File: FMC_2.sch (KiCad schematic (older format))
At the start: 14 parts, among them P2 SAMTEC_ASP-134603-01

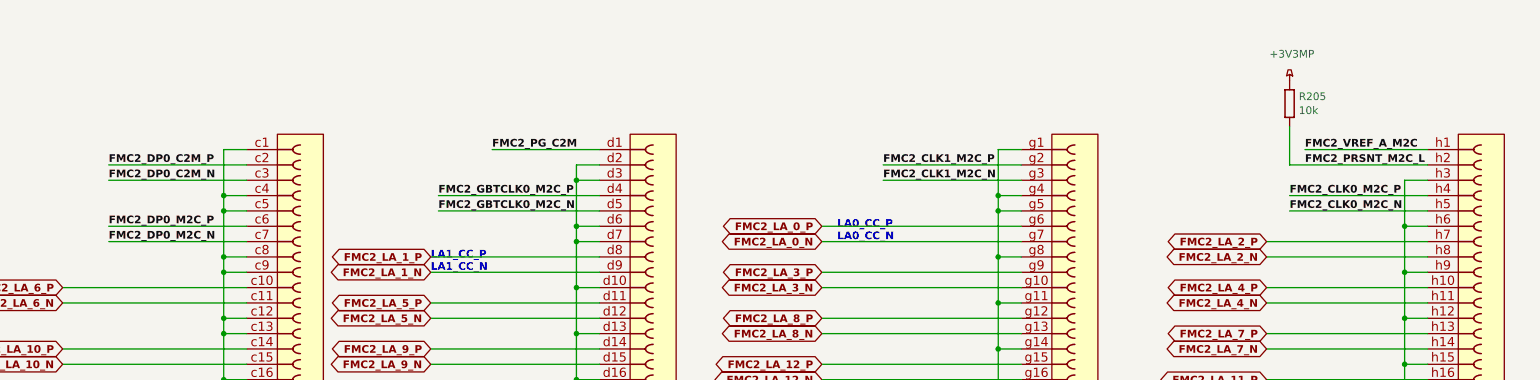
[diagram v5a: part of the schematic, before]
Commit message: new FMC JTAG chain
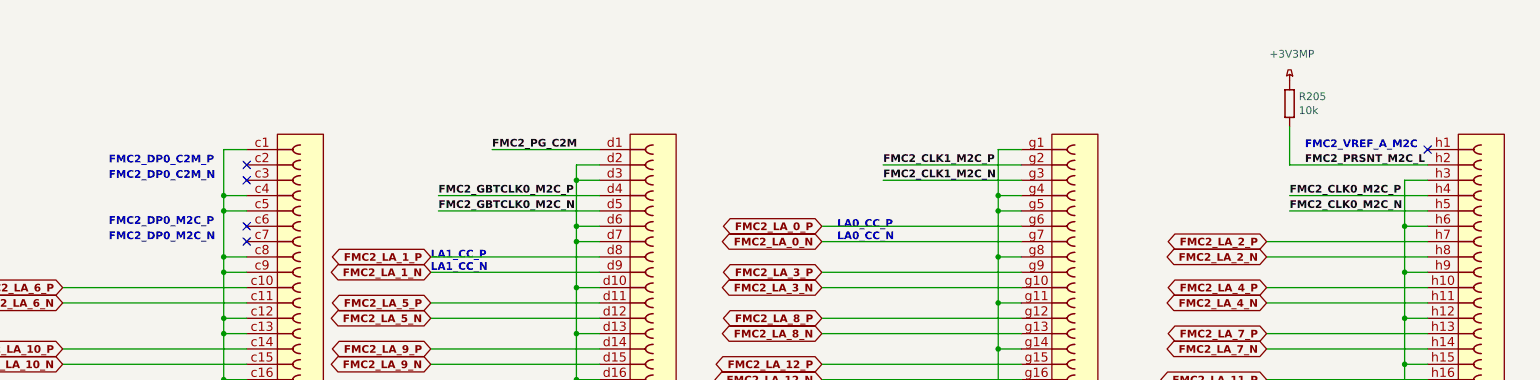
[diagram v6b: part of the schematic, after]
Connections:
- net FMC2_DP0_C2M_N: no longer names the net of P2.c3
- net FMC2_DP0_C2M_P: no longer names the net of P2.c2
- net FMC2_DP0_M2C_N: no longer names the net of P2.c7
- net FMC2_DP0_M2C_P: no longer names the net of P2.c6
- net FMC2_VREF_A_M2C: no longer names the net of P2.h1
- no-connect marks 0 -> 5
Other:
- note added: "FMC2_DP0_C2M_N"
- note added: "FMC2_DP0_C2M_P"
- note added: "FMC2_DP0_M2C_N"
- note added: "FMC2_DP0_M2C_P"
- note added: "FMC2_VREF_A_M2C"
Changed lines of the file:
@@
 Wire Wire Line
 	11400 5450 11400 5750
-Text Label 2950 2050 0    50   ~ 10
-FMC2_DP0_C2M_P
-Text Label 2950 2150 0    50   ~ 10
-FMC2_DP0_C2M_N
-Text Label 2950 2450 0    50   ~ 10
-FMC2_DP0_M2C_P
-Text Label 2950 2550 0    50   ~ 10
-FMC2_DP0_M2C_N
 Text Label 3150 4050 0    50   ~ 10
 FMC2_P_LA_18
@@
 Wire Wire Line
 	3150 4950 3850 4950
-Wire Wire Line
-	2950 2050 3850 2050
-Wire Wire Line
-	2950 2150 3850 2150
-Wire Wire Line
-	2950 2450 3850 2450
-Wire Wire Line
-	2950 2550 3850 2550
 Text Notes 2700 4150 0    50   ~ 10
 LA18_CC_P\nLA18_CC_N
@@
 Text Label 5450 5150 0    50   ~ 10
 FMC2_TMS
-Text Label 5450 5250 0    50   ~ 10
-FMC2_TRST
 Text Label 5450 5350 0    50   ~ 10
 GA1_2
@@
 Wire Wire Line
 	5450 5150 6150 5150
-Wire Wire Line
-	5450 5250 6150 5250
 Wire Wire Line
 	5450 5350 6150 5350
@@
 Text Label 8000 2150 0    50   ~ 10
 FMC2_CLK1_M2C_N
-Text Label 10750 1950 0    50   ~ 10
-FMC2_VREF_A_M2C
 Text Label 10750 2050 0    50   ~ 10
 FMC2_PRSNT_M2C_L
@@
 Wire Wire Line
 	8000 2150 8900 2150
-Wire Wire Line
-	10750 1950 11550 1950
 Wire Wire Line
 	10650 2250 11550 2250
@@
 	-1   0    0    1
 $EndComp
+Text Notes 2950 2050 0    50   ~ 10
+FMC2_DP0_C2M_P
+Text Notes 2950 2150 0    50   ~ 10
+FMC2_DP0_C2M_N
+Text Notes 2950 2450 0    50   ~ 10
+FMC2_DP0_M2C_P
+Text Notes 2950 2550 0    50   ~ 10
+FMC2_DP0_M2C_N
+NoConn ~ 3850 2050
+NoConn ~ 3850 2150
+NoConn ~ 3850 2450
+NoConn ~ 3850 2550
+NoConn ~ 11550 1950
+Text Notes 10750 1950 0    50   ~ 10
+FMC2_VREF_A_M2C
+Text Label 5450 5250 0    50   ~ 10
+FMC2_TRST
+Wire Wire Line
+	5450 5250 6150 5250
 $EndSCHEMATC

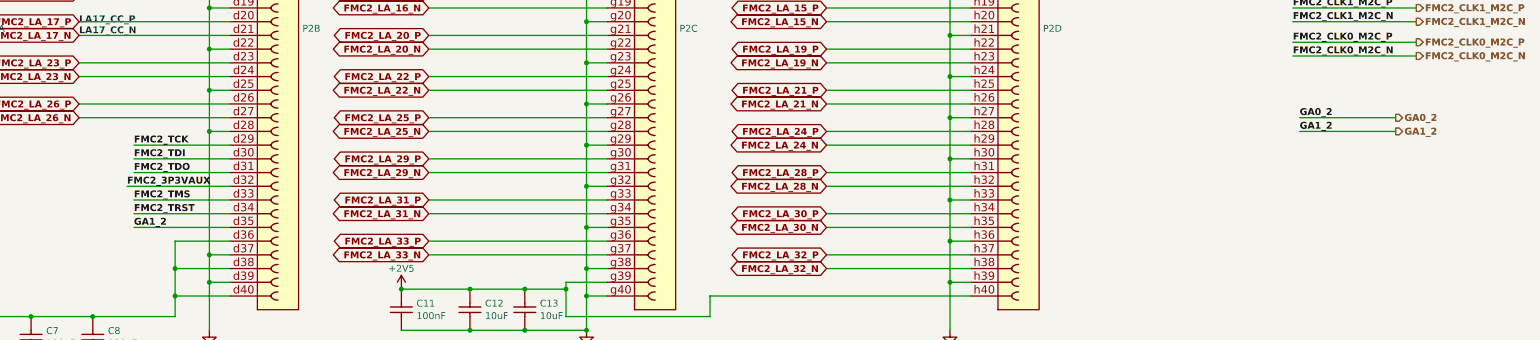
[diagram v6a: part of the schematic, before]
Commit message: JTAG improvrmrnt, bugs fixed
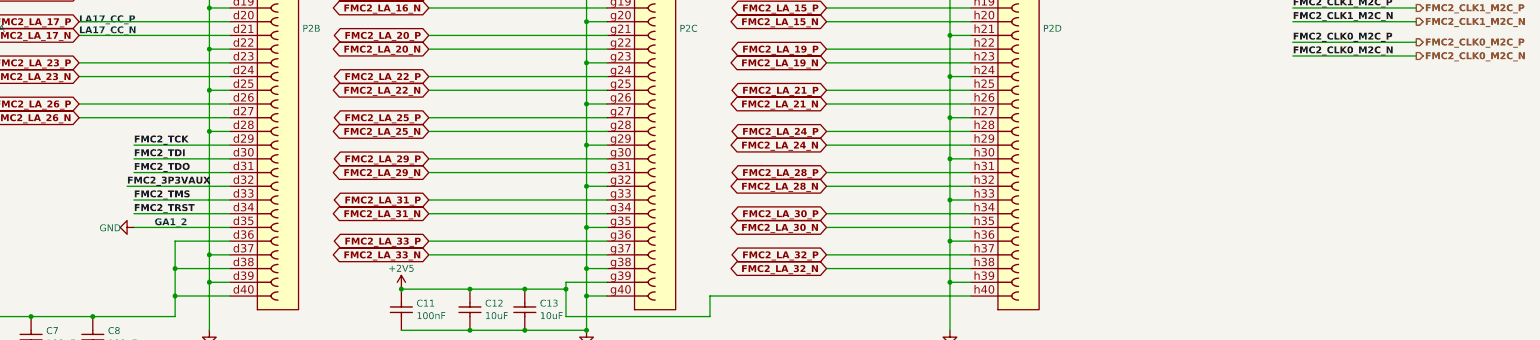
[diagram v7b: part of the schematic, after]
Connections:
- net GA1_2 is gone; now on net GND: P2.d35
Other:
- note added: "GA1_2"
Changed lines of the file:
@@
 Comp "Michał Gąska / WUT"
 Comment1 ""
-Comment2 "FMC 2 connector"
-Comment3 ""
+Comment2 ""
+Comment3 "FMC 2 connector"
 Comment4 ""
 $EndDescr
@@
 Text Label 5450 5150 0    50   ~ 10
 FMC2_TMS
-Text Label 5450 5350 0    50   ~ 10
-GA1_2
 Wire Wire Line
 	5450 1950 6150 1950
@@
 Wire Wire Line
 	13900 4100 14800 4100
-Text Label 13950 4550 0    50   ~ 10
-GA0_2
-Wire Wire Line
-	13950 4550 14650 4550
-Text Label 13950 4650 0    50   ~ 10
-GA1_2
-Wire Wire Line
-	13950 4650 14650 4650
 Text HLabel 14800 3500 2    50   Output ~ 10
 FMC2_GBTCLK0_M2C_P
@@
 	1    0    0    -1
 $EndComp
-Text HLabel 14650 4550 2    50   Output ~ 10
-GA0_2
-Text HLabel 14650 4650 2    50   Output ~ 10
-GA1_2
 Wire Wire Line
 	7150 6900 7300 6900
@@
 	0    1    1    0
 $EndComp
-Text Notes 2900 5250 0    50   ~ 10
-GA0_2
-Text Label 3150 5250 0    50   ~ 10
-FMC2_3P3VAUX
 Text HLabel 4800 6900 0    50   Output ~ 0
 FMC2_FUSE
@@
 Wire Wire Line
 	5450 5250 6150 5250
+Text Label 3150 5250 0    50   ~ 10
+FMC2_3P3VAUX
+Text Notes 2900 5250 0    50   ~ 10
+GA0_2
+$Comp
+L power:GND #PWR?
+U 1 1 5D1DC9A3
+P 5450 5350
+AR Path="/5BD32060/5D1DC9A3" Ref="#PWR?"  Part="1"
+AR Path="/5BD31F9A/5D1DC9A3" Ref="#PWR?"  Part="1"
+AR Path="/5BD31F9F/5D1DC9A3" Ref="#PWR?"  Part="1"
+AR Path="/5D1DC9A3" Ref="#PWR?"  Part="1"
+F 0 "#PWR?" H 5450 5100 50  0001 C CNN
+F 1 "GND" V 5455 5177 50  0000 C CNN
+F 2 "" H 5450 5350 50  0001 C CNN
+F 3 "" H 5450 5350 50  0001 C CNN
+	1    5450 5350
+	0    1    1    0
+$EndComp
+Text Notes 5600 5350 0    50   ~ 10
+GA1_2
 $EndSCHEMATC
